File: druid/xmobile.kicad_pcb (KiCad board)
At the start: 4 copper layers, 41.9 x 61.8 mm, 143 parts, among them J1 Micro_SD_Card, J2 TEST_VIBRO, J3 TEST_DISP_DATA_OUT, J4 USB_B_Micro, P1 CONN_8, Q1 BC850, Q2 BC850, SW1 SW_PUSH, SW10 SW_PUSH, SW11 SW_PUSH, SW12 SW_PUSH, SW13 SW_PUSH, SW14 SW_PUSH, SW15 SW_PUSH, SW16 SW_PUSH, SW17 SW_PUSH, SW18 SW_PUSH, SW19 SW_PUSH, SW2 SW_PUSH, SW20 SW_PUSH, SW21 SW_PUSH, SW3 SW_PUSH, SW4 SW_PUSH, SW5 SW_PUSH, SW6 SW_PUSH, SW7 SW_PUSH, SW8 SW_PUSH, SW9 SW_PUSH, U1 CY62158EV30LL-45BVXI, U2 XMega128A1U_BGA100, U3 TP4056, U4 TP4056, U5 XC6206P332MR, U6 MAX7370, U7 78646-3001, U8 SIM800C, U9 STF202-22T1G

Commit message: KBD controller and SRAM packages changed from BGA to ... TSOP and TQFN XMEGA packaged need to be changed
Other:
- copper layers 4 -> 8
- net class Default: trace_width 0.25 -> 0.15
- rule trace_min: 0.2 -> 0.15
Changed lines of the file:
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@@
     (1 In1.Cu signal hide)
     (2 In2.Cu signal hide)
+    (3 In3.Cu signal hide)
+    (4 In4.Cu signal hide)
+    (5 In5.Cu signal hide)
+    (6 In6.Cu signal hide)
     (31 B.Cu signal)
     (32 B.Adhes user hide)
@@
     (34 B.Paste user hide)
     (35 F.Paste user hide)
-    (36 B.SilkS user hide)
+    (36 B.SilkS user)
     (37 F.SilkS user hide)
     (38 B.Mask user hide)
@@
   )
   (setup
-    (last_trace_width 0.25)
+    (last_trace_width 0.15)
     (trace_clearance 0.2)
     (zone_clearance 0.508)
     (zone_45_only no)
-    (trace_min 0.2)
+    (trace_min 0.15)
     (segment_width 0.2)
     (edge_width 0.1)
@@
   (net_class Default "This is the default net class."
     (clearance 0.2)
-    (trace_width 0.25)
+    (trace_width 0.15)
     (via_dia 0.8)
     (via_drill 0.4)

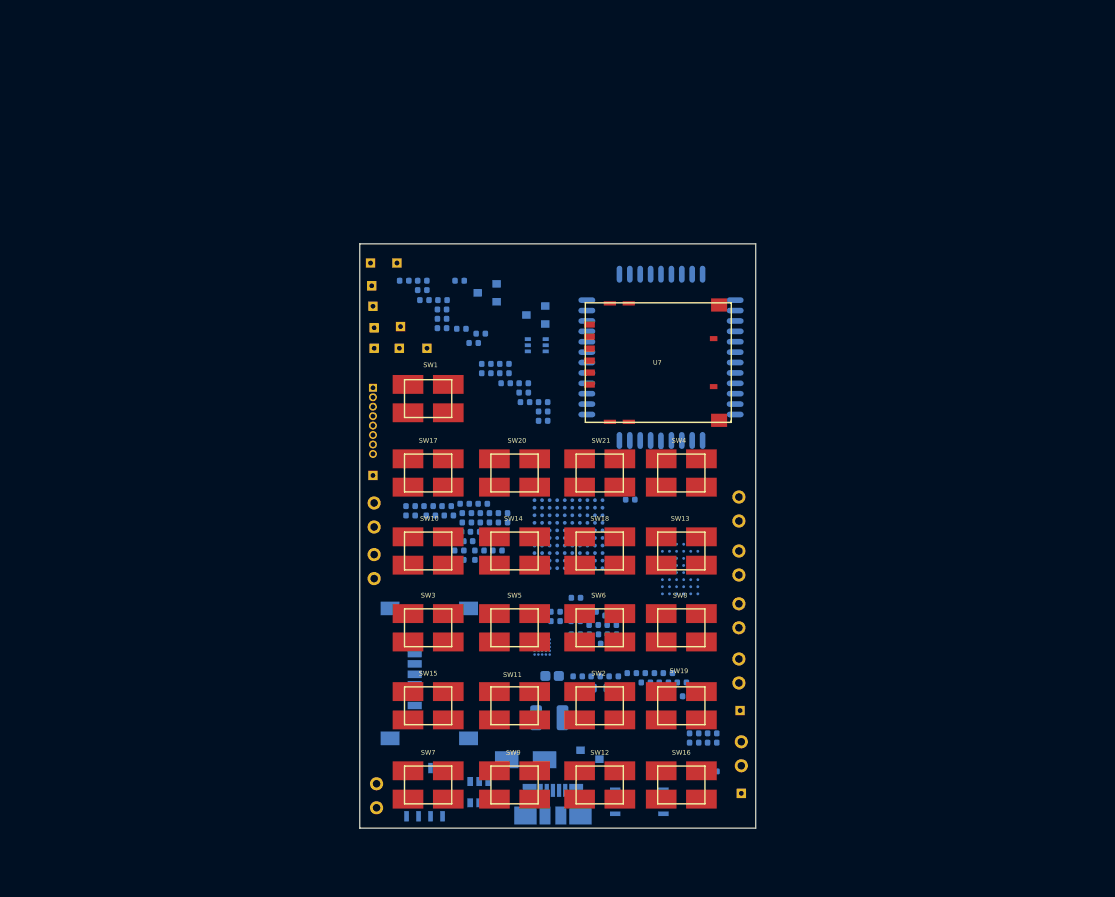
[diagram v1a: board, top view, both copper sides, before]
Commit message: Done with packages. Start to place components.
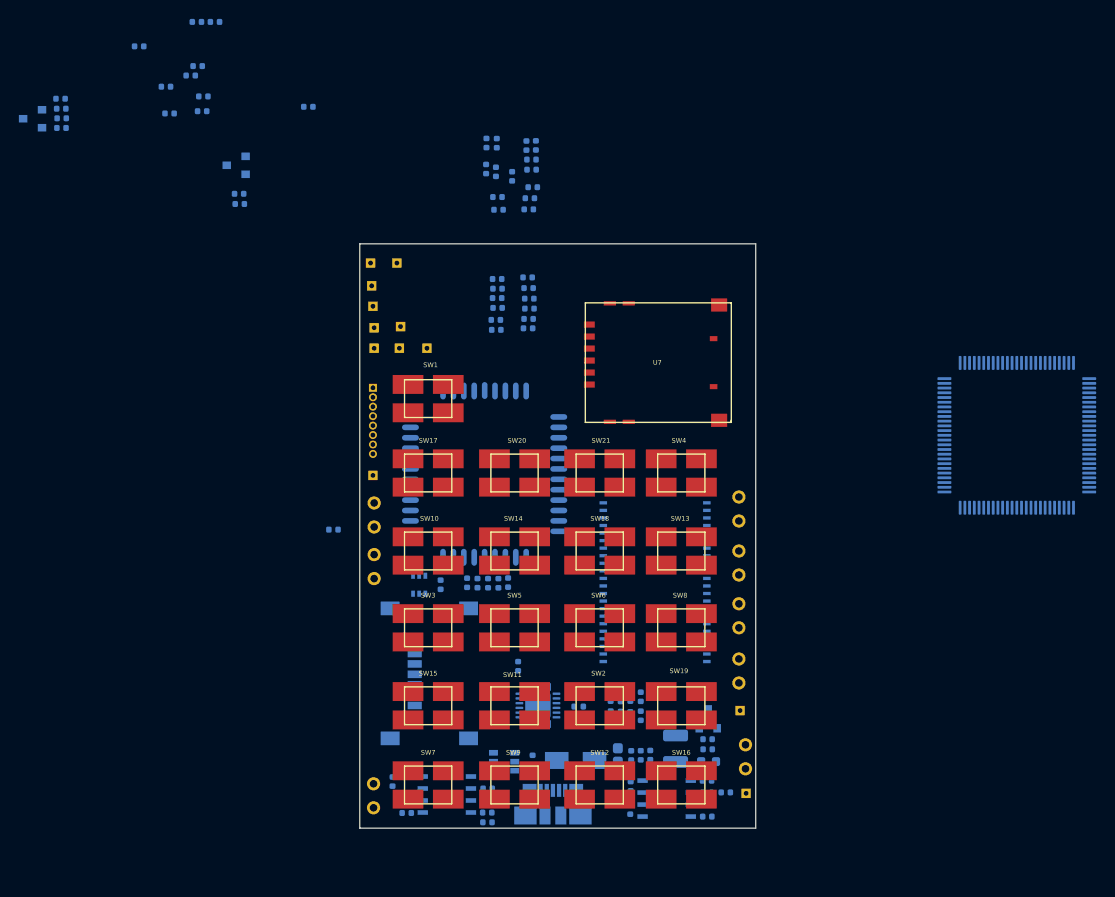
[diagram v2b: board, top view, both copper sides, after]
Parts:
- removed 1u1, 1u2: C, Capacitor_SMD:C_0402_1005Metric
- added C1: 1u, Capacitor_SMD:C_0402_1005Metric, B.Cu at (168.7, 119.7)
- added C35: 1u, Capacitor_SMD:C_0402_1005Metric, B.Cu at (168.7, 120.8)
- U1: value CY62158EV30LL-45BVXI -> CY62158EV30LL-45ZSXIT; footprint druid:48-ball_VFBGA_6x8x1mm_BV48BZ48 -> druid:TSOPII_44_pin
- U2: value XMega128A1U_BGA100 -> XMega128A1U_TQFP100; footprint druid:BGA100_9x9x1.2_pitch-0.80mm -> Package_QFP:TQFP-100_14x14mm_P0.5mm
- U6: footprint druid:W252F2+1_21-0453 -> Package_DFN_QFN:QFN-24-1EP_4x4mm_P0.5mm_EP2.7x2.7mm
- moved Q2 51.5 mm to (110.9, 59.7)
- moved U2 48.6 mm to (215.1, 93.2)
- moved R21 48.5 mm to (125.4, 59.1)
- moved R33 48.3 mm to (113.9, 58.6)
- moved D19 46.4 mm to (113.9, 57.5)
- moved R32 45.1 mm to (114.0, 59.6)
- moved D7 43.1 mm to (159.0, 62.2), turned to 270 degrees
- moved R26 42.3 mm to (128.9, 58.9)
- moved R31 41.9 mm to (114.0, 60.6)
- moved R24 41.2 mm to (128.4, 54.1)
- moved R23 41.2 mm to (127.6, 55.1)
- moved R27 41.2 mm to (129.0, 57.3)
- moved C19 40.2 mm to (163.7, 64.0), turned to 180 degrees
- moved R30 39.6 mm to (132.8, 67.6)
- moved D3 39.5 mm to (160.0, 62.2), turned to 90 degrees
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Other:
- net class Default: trace_width 0.15 -> 0.25
- rule trace_min: 0.15 -> 0.2

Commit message: Continue layout
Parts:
- added REF**: 1pin, Connectors:1pin, F.Cu at (145.4, 87.8)
- added REF**: 1pin, Connectors:1pin, F.Cu at (187.4, 95.6)
- added REF**: 1pin, Connectors:1pin, F.Cu at (178.7, 137.7)
- added REF**: 1pin, Connectors:1pin, F.Cu at (152.0, 137.1)
- moved R22 63.6 mm to (169.0, 98.2)
- moved R20 61.6 mm to (169.0, 97.2), turned to 0 degrees
- moved R24 58.4 mm to (168.9, 96.2), turned to 0 degrees
- moved R23 57.5 mm to (168.9, 95.1), turned to 0 degrees
- moved R19 56.6 mm to (168.4, 92.6), turned to 90 degrees
- moved R21 55.9 mm to (169.4, 93.6), turned to 90 degrees
- moved R28 51.9 mm to (163.3, 83.7)
- moved R25 50.0 mm to (169.0, 99.3), turned to 0 degrees
- moved R27 42.1 mm to (163.3, 81.7)
- moved R26 41.9 mm to (163.3, 82.7)
- moved U2 39.2 mm to (177.2, 83.2)
- moved C5 32.3 mm to (163.5, 108.7), turned to 270 degrees
- moved C3 31.8 mm to (164.1, 110.2)
- moved C4 31.4 mm to (164.5, 108.7), turned to 90 degrees
- moved C6 31.1 mm to (166.0, 110.2), turned to 180 degrees
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
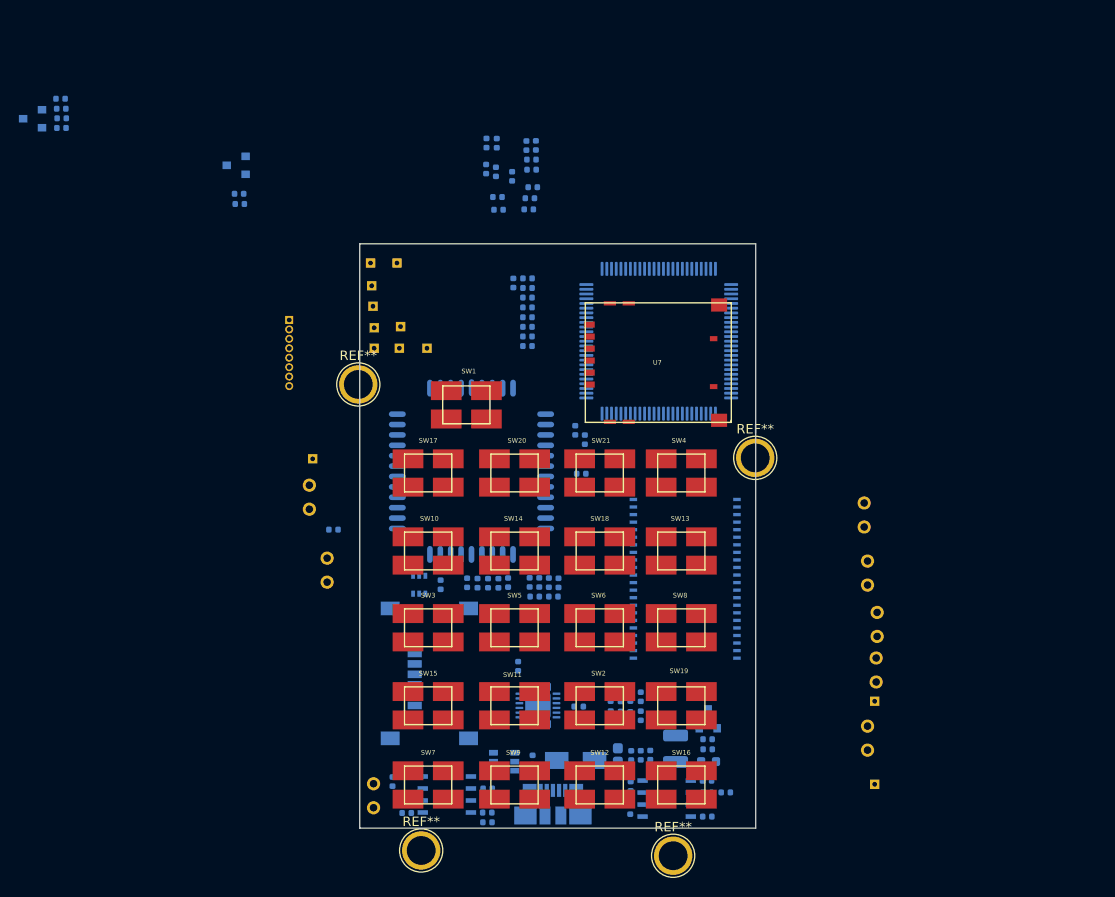
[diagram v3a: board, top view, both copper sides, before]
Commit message: Route completed. 149 vias.
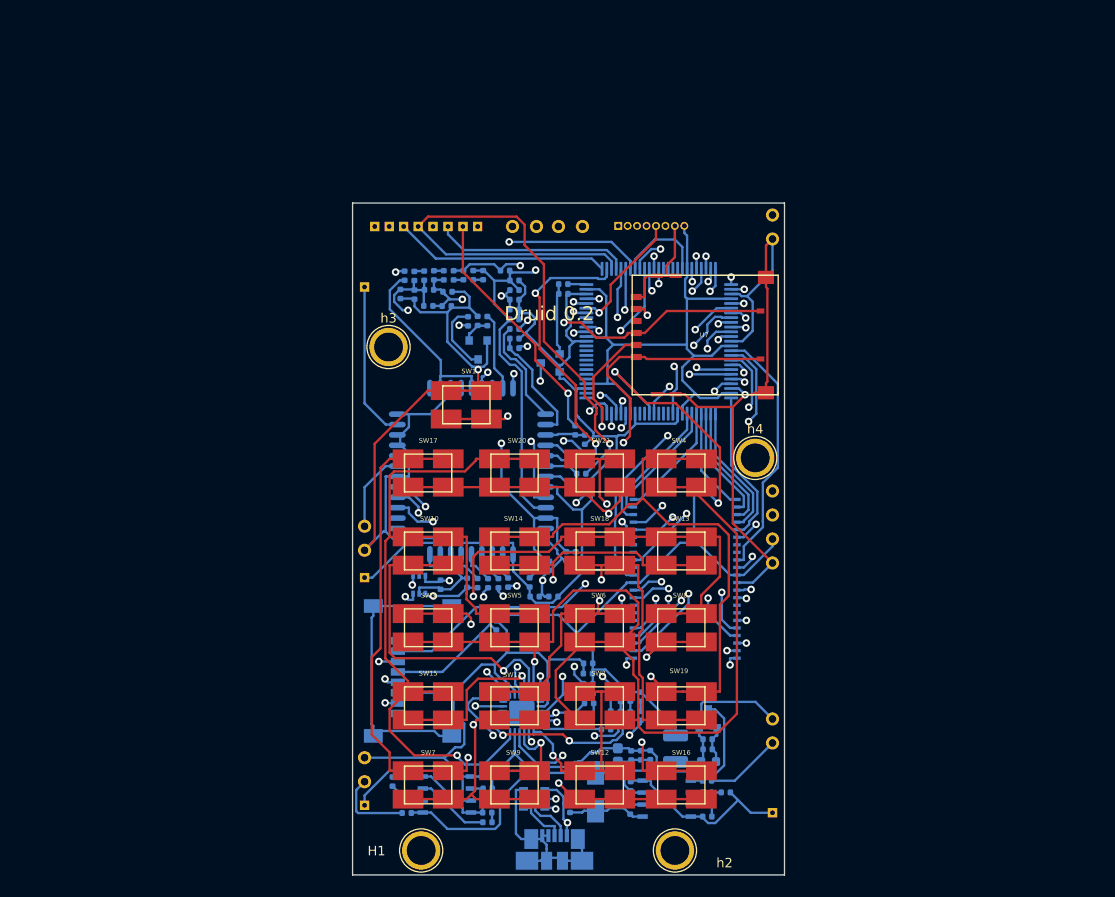
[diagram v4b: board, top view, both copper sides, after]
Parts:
- removed REF** (x4): 1pin, Connectors:1pin
- added H1: 1pin, Connectors:1pin, F.Cu at (152.0, 137.1)
- added h2: 1pin, Connectors:1pin, F.Cu at (178.9, 137.1)
- added h3: 1pin, Connectors:1pin, F.Cu at (148.6, 83.8)
- added h4: 1pin, Connectors:1pin, F.Cu at (187.4, 95.6)
- moved W3 64.6 mm to (166.6, 71.1), turned to 0 degrees
- moved W8 55.2 mm to (146.1, 129.8)
- moved W6 55.1 mm to (146.1, 132.3)
- moved Q2 53.1 mm to (158.1, 84.1), turned to 270 degrees
- moved W17 52.9 mm to (146.1, 102.8)
- moved R31 49.5 mm to (159.0, 81.1), turned to 270 degrees
- moved W2 49.0 mm to (189.2, 101.6)
- moved R32 49.0 mm to (158.0, 81.1), turned to 270 degrees
- moved R33 48.6 mm to (157.0, 81.1), turned to 270 degrees
- moved W4 43.7 mm to (164.2, 71.1), turned to 180 degrees
- moved D19 41.0 mm to (150.3, 76.3), turned to 270 degrees
- moved Q1 39.3 mm to (165.7, 85.5)
- moved R1 38.8 mm to (181.2, 98.2)
- moved J2 38.0 mm to (189.2, 72.4)
- moved P1 36.2 mm to (172.9, 71.0), turned to 270 degrees
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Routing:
- net GND: track 0.00 -> 472.5 mm, vias 0 -> 2
- net 3.3V: track 0.00 -> 232.8 mm, vias 0 -> 2
- net /xmobile_keyboard/C0: track 0.00 -> 108.4 mm, vias 0 -> 1
- net /xmobile_keyboard/C1: track 0.00 -> 93.3 mm, vias 0 -> 3
- net /xmobile_keyboard/R2: track 0.00 -> 89.5 mm, vias 0 -> 2
- net /xmobile_keyboard/R3: track 0.00 -> 88.5 mm, vias 0 -> 1
- net /xmobile_keyboard/C2: track 0.00 -> 84.7 mm, vias 0 -> 3
- net /xmobile_keyboard/R0: track 0.00 -> 84.1 mm, vias 0 -> 2
- net /xmobile_keyboard/R4: track 0.00 -> 82.5 mm, vias 0 -> 4
- net /xmobile_keyboard/C3: track 0.00 -> 80.0 mm, vias 0 -> 3
- net /xmobile_keyboard/R1: track 0.00 -> 73.5 mm, vias 0 -> 3
- net Net-(D18-Pad3): track 0.00 -> 72.1 mm, vias 0 -> 3
- net /microSD_SCLK: track 0.00 -> 67.8 mm, vias 0 -> 2
- net /GSM_RI: track 0.00 -> 67.7 mm, vias 0 -> 1
- net /audio/AUDIO_SPKN: track 0.00 -> 67.2 mm, vias 0 -> 2
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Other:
- board size 41.9 x 61.8 mm -> 45.7 x 71.1 mm
- copper layers 8 -> 4
- board text added: "Druid 0.2"

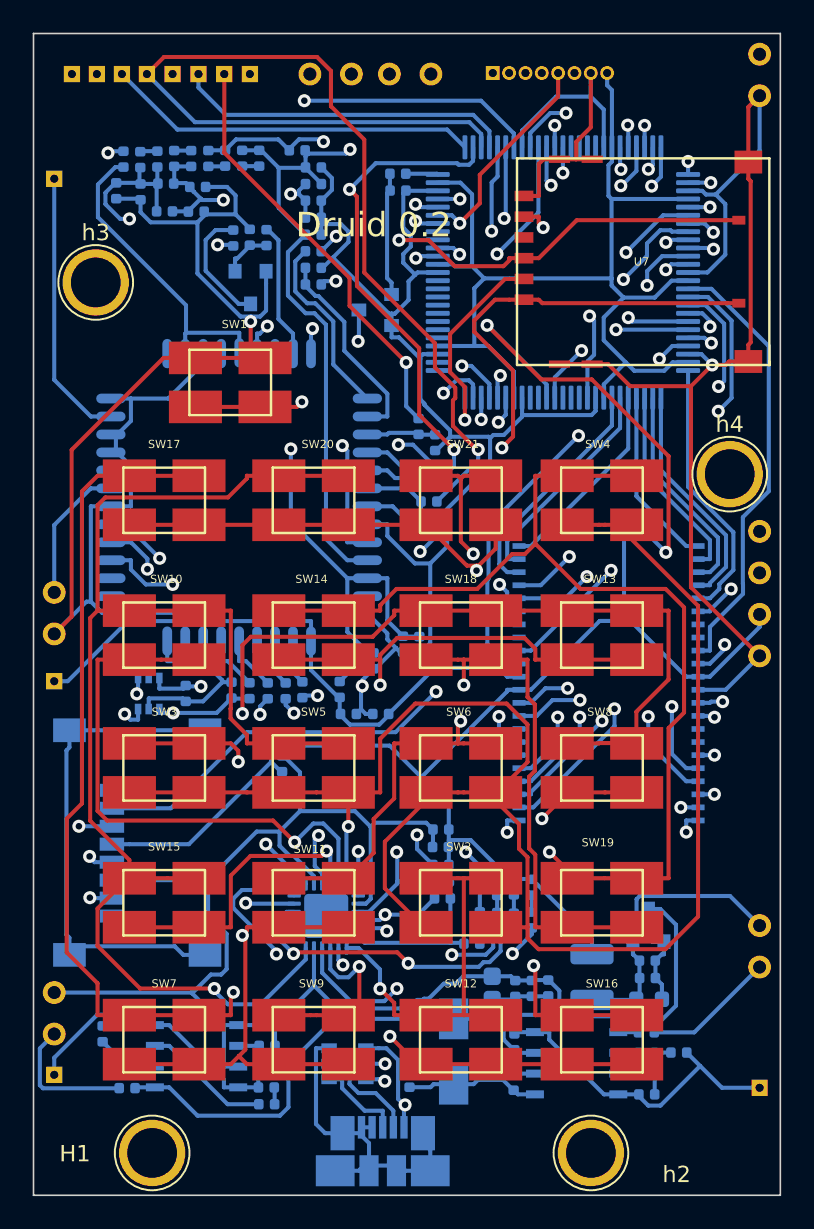
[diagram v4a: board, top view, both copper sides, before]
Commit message: Added filled zones
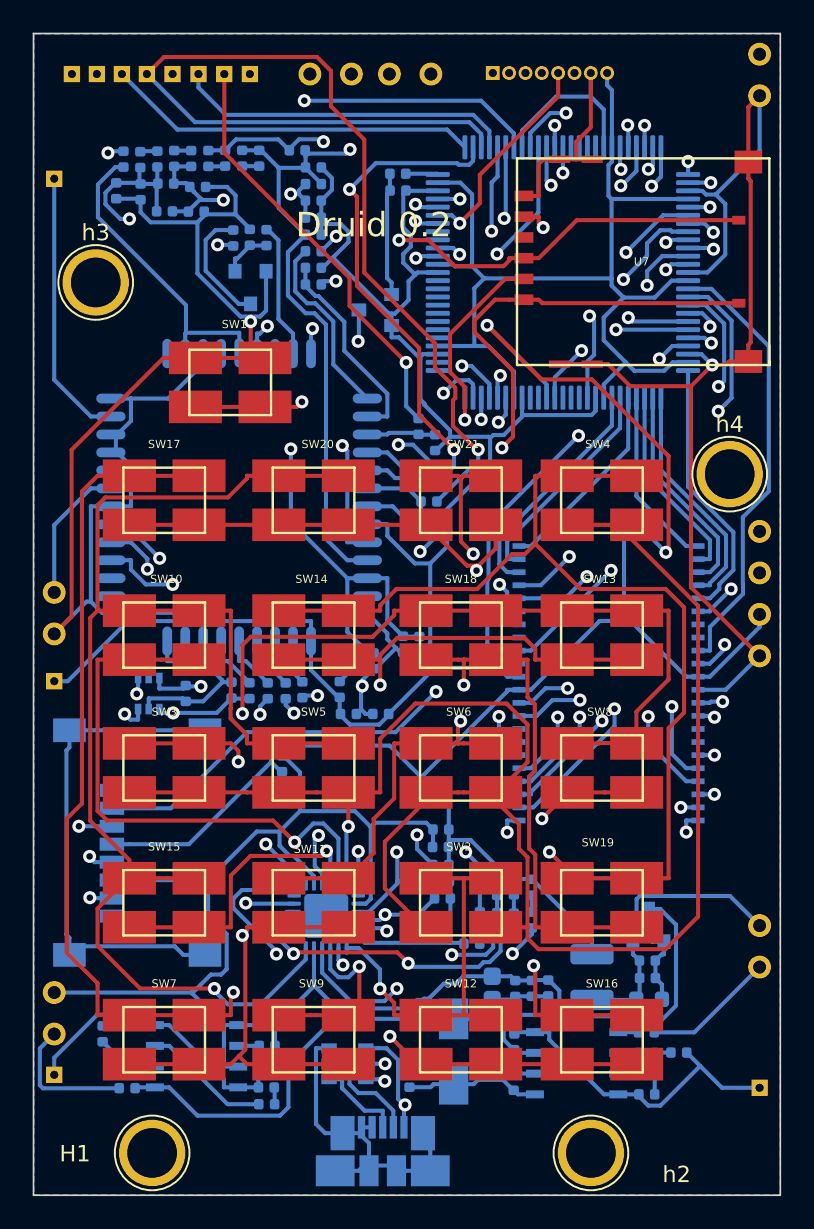
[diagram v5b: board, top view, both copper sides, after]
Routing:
- added copper zone on B.Cu, net GND
- added copper zone on F.Cu, net GND
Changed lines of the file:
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@@
   (page A4)
   (layers
-    (0 F.Cu signal hide)
-    (1 In1.Cu signal hide)
-    (2 In2.Cu signal hide)
+    (0 F.Cu signal)
+    (1 In1.Cu signal)
+    (2 In2.Cu signal)
     (31 B.Cu signal)
     (32 B.Adhes user hide)
@@
   (segment (start 146.05 77.47) (end 146.05 89.7837) (width 0.25) (layer B.Cu) (net 134))
   (segment (start 146.05 89.7837) (end 148.2927 92.0264) (width 0.25) (layer B.Cu) (net 134))
+  (zone (net 2) (net_name GND) (layer F.Cu) (hatch edge 0.508)
+    (connect_pads (clearance 0.508))
+    (min_thickness 0.254)
+    (fill yes (arc_segments 16) (thermal_gap 0.508) (thermal_bridge_width 0.508))
+    (polygon
+      (pts
+        (xy 144.8 68.6) (xy 144.8 139.7) (xy 190.5 139.7) (xy 190.5 68.6)
+      )
+    )
+  )
+  (zone (net 2) (net_name GND) (layer B.Cu) (hatch edge 0.508)
+    (connect_pads (clearance 0.508))
+    (min_thickness 0.254)
+    (fill yes (arc_segments 16) (thermal_gap 0.508) (thermal_bridge_width 0.508))
+    (polygon
+      (pts
+        (xy 144.8 68.6) (xy 144.8 139.7) (xy 190.5 139.7) (xy 190.5 68.6)
+      )
+    )
+  )
 )

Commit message: fix pcb issues.board completed.
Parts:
- removed P1: CONN_8, Connector_PinHeader_1.00mm:PinHeader_1x08_P1.00mm_Vertical
- added J10: EPD_1, TestPoint:TestPoint_THTPad_1.0x1.0mm_Drill0.5mm, F.Cu at (174.8, 70.0)
- added J11: EPD_1, TestPoint:TestPoint_THTPad_1.0x1.0mm_Drill0.5mm, F.Cu at (173.7, 70.0)
- added J12: EPD_1, TestPoint:TestPoint_THTPad_1.0x1.0mm_Drill0.5mm, F.Cu at (172.4, 70.0)
- added J5: EPD_1, TestPoint:TestPoint_THTPad_1.0x1.0mm_Drill0.5mm, F.Cu at (180.8, 70.0)
- added J6: EPD_1, TestPoint:TestPoint_THTPad_1.0x1.0mm_Drill0.5mm, F.Cu at (179.7, 70.0)
- added J7: EPD_1, TestPoint:TestPoint_THTPad_1.0x1.0mm_Drill0.5mm, F.Cu at (178.4, 70.0)
- added J8: EPD_1, TestPoint:TestPoint_THTPad_1.0x1.0mm_Drill0.5mm, F.Cu at (177.2, 70.0)
- added J9: EPD_1, TestPoint:TestPoint_THTPad_1.0x1.0mm_Drill0.5mm, F.Cu at (176.1, 70.0)
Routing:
- net 3.3V: track 232.8 -> 187.1 mm, vias 2 -> 1
- net /xmobile_keyboard/C0: track 108.4 -> 89.8 mm
- net /GSM_RXD: track 41.1 -> 55.6 mm, vias 2 -> 1
- net /GSM_TXD: track 38.4 -> 51.4 mm, vias 2 -> 1
- net /xmobile_keyboard/R3: track 88.5 -> 78.2 mm, vias 1 -> 2
- net /GSM_CTS: track 58.6 -> 50.6 mm
- net /microSD_SCLK: track 67.8 -> 59.9 mm
- net /xmobile_keyboard/C2: track 84.7 -> 92.5 mm
- net GND: track 472.5 -> 479.2 mm, vias 2 -> 5
- net Net-(C32-Pad1): track 48.7 -> 43.4 mm
- net /EPD_RST: track 26.8 -> 21.8 mm
- net /GSM_RI: track 67.7 -> 62.8 mm
- net /PDI_C: track 57.2 -> 52.3 mm, vias 3 -> 2
- net Net-(D18-Pad3): track 72.1 -> 67.2 mm
- net Net-(C33-Pad1): track 53.3 -> 48.7 mm
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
